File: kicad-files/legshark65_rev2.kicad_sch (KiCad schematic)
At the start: 199 parts, among them J1 ARM JTAG, SW1 K2-1187SQ-A4SW-06, SW2 PCM12SMTR, T2 53261-0471, U1 STM32F411CEU6, U2 MCP1700T-3302E/TT, U3 AT24C256C-SSHL-T, Y1 TAXM8M4RFDCET2T

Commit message: Started connecting more stuff
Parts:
- C1, C10, C11, C12, C13, C14, C15, C17, C2, C6, C7, C9: footprint Capacitor_SMD:C_0603_1608Metric_Pad1.08x0.95mm_HandSolder -> Capacitor_SMD:C_0402_1005Metric_Pad0.74x0.62mm_HandSolder
- C3, C5: footprint Capacitor_SMD:C_0603_1608Metric -> Capacitor_SMD:C_0402_1005Metric_Pad0.74x0.62mm_HandSolder
- R1, R11, R15, R5, R6, R7, R8: footprint Resistor_SMD:R_0603_1608Metric -> Resistor_SMD:R_0402_1005Metric_Pad0.72x0.64mm_HandSolder
- R4, R9: footprint Resistor_SMD:R_0402_1005Metric -> Resistor_SMD:R_0402_1005Metric_Pad0.72x0.64mm_HandSolder
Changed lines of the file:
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@@
       (effects (font (size 1.27 1.27)) (justify left))
     )
-    (property "Footprint" "Capacitor_SMD:C_0603_1608Metric_Pad1.08x0.95mm_HandSolder" (at 116.205 205.4352 0)
+    (property "Footprint" "Capacitor_SMD:C_0402_1005Metric_Pad0.74x0.62mm_HandSolder" (at 116.205 205.4352 0)
       (effects (font (size 1.27 1.27)) hide)
     )
@@
       (effects (font (size 1.27 1.27)) (justify left))
     )
-    (property "Footprint" "Capacitor_SMD:C_0603_1608Metric_Pad1.08x0.95mm_HandSolder" (at 104.14 227.6348 0)
+    (property "Footprint" "Capacitor_SMD:C_0402_1005Metric_Pad0.74x0.62mm_HandSolder" (at 104.14 227.6348 0)
       (effects (font (size 1.27 1.27)) hide)
     )
@@
       (effects (font (size 1.27 1.27)) (justify left))
     )
-    (property "Footprint" "Capacitor_SMD:C_0603_1608Metric_Pad1.08x0.95mm_HandSolder" (at 134.62 188.9252 0)
+    (property "Footprint" "Capacitor_SMD:C_0402_1005Metric_Pad0.74x0.62mm_HandSolder" (at 134.62 188.9252 0)
       (effects (font (size 1.27 1.27)) hide)
     )
@@
       (effects (font (size 1.27 1.27)))
     )
-    (property "Footprint" "Resistor_SMD:R_0603_1608Metric" (at 180.848 289.56 90)
+    (property "Footprint" "Resistor_SMD:R_0402_1005Metric_Pad0.72x0.64mm_HandSolder" (at 180.848 289.56 90)
       (effects (font (size 1.27 1.27)) hide)
     )
@@
       (effects (font (size 1.27 1.27)) (justify left))
     )
-    (property "Footprint" "Capacitor_SMD:C_0603_1608Metric_Pad1.08x0.95mm_HandSolder" (at 204.47 297.4848 0)
+    (property "Footprint" "Capacitor_SMD:C_0402_1005Metric_Pad0.74x0.62mm_HandSolder" (at 204.47 297.4848 0)
       (effects (font (size 1.27 1.27)) hide)
     )
@@
       (effects (font (size 1.27 1.27)))
     )
-    (property "Footprint" "Resistor_SMD:R_0603_1608Metric" (at 99.06 182.118 90)
+    (property "Footprint" "Resistor_SMD:R_0402_1005Metric_Pad0.72x0.64mm_HandSolder" (at 99.06 182.118 90)
       (effects (font (size 1.27 1.27)) hide)
     )
@@
       (effects (font (size 1.27 1.27)))
     )
-    (property "Footprint" "Resistor_SMD:R_0603_1608Metric" (at 232.41 222.758 90)
+    (property "Footprint" "Resistor_SMD:R_0402_1005Metric_Pad0.72x0.64mm_HandSolder" (at 232.41 222.758 90)
       (effects (font (size 1.27 1.27)) hide)
     )
@@
       (effects (font (size 1.27 1.27)) (justify left))
     )
-    (property "Footprint" "Capacitor_SMD:C_0603_1608Metric" (at 50.4952 298.45 0)
+    (property "Footprint" "Capacitor_SMD:C_0402_1005Metric_Pad0.74x0.62mm_HandSolder" (at 50.4952 298.45 0)
       (effects (font (size 1.27 1.27)) hide)
     )
@@
       (effects (font (size 1.27 1.27)))
     )
-    (property "Footprint" "Resistor_SMD:R_0402_1005Metric" (at 57.658 294.64 90)
+    (property "Footprint" "Resistor_SMD:R_0402_1005Metric_Pad0.72x0.64mm_HandSolder" (at 57.658 294.64 90)
       (effects (font (size 1.27 1.27)) hide)
     )
@@
       (effects (font (size 1.27 1.27)))
     )
-    (property "Footprint" "Resistor_SMD:R_0402_1005Metric" (at 94.488 294.64 90)
+    (property "Footprint" "Resistor_SMD:R_0402_1005Metric_Pad0.72x0.64mm_HandSolder" (at 94.488 294.64 90)
       (effects (font (size 1.27 1.27)) hide)
     )
@@
       (effects (font (size 1.27 1.27)) (justify left))
     )
-    (property "Footprint" "Capacitor_SMD:C_0603_1608Metric_Pad1.08x0.95mm_HandSolder" (at 192.7352 293.37 0)
+    (property "Footprint" "Capacitor_SMD:C_0402_1005Metric_Pad0.74x0.62mm_HandSolder" (at 192.7352 293.37 0)
       (effects (font (size 1.27 1.27)) hide)
     )
@@
       (effects (font (size 1.27 1.27)) (justify left))
     )
-    (property "Footprint" "Capacitor_SMD:C_0603_1608Metric_Pad1.08x0.95mm_HandSolder" (at 106.9848 180.34 0)
+    (property "Footprint" "Capacitor_SMD:C_0402_1005Metric_Pad0.74x0.62mm_HandSolder" (at 106.9848 180.34 0)
       (effects (font (size 1.27 1.27)) hide)
     )
@@
       (effects (font (size 1.27 1.27)))
     )
-    (property "Footprint" "Resistor_SMD:R_0603_1608Metric" (at 100.33 156.972 90)
+    (property "Footprint" "Resistor_SMD:R_0402_1005Metric_Pad0.72x0.64mm_HandSolder" (at 100.33 156.972 90)
       (effects (font (size 1.27 1.27)) hide)
     )
@@
       (effects (font (size 1.27 1.27)) (justify left))
     )
-    (property "Footprint" "Capacitor_SMD:C_0603_1608Metric_Pad1.08x0.95mm_HandSolder" (at 96.52 235.2548 0)
+    (property "Footprint" "Capacitor_SMD:C_0402_1005Metric_Pad0.74x0.62mm_HandSolder" (at 96.52 235.2548 0)
       (effects (font (size 1.27 1.27)) hide)
     )
@@
       (effects (font (size 1.27 1.27)) (justify left))
     )
-    (property "Footprint" "Capacitor_SMD:C_0603_1608Metric_Pad1.08x0.95mm_HandSolder" (at 107.6452 256.54 0)
+    (property "Footprint" "Capacitor_SMD:C_0402_1005Metric_Pad0.74x0.62mm_HandSolder" (at 107.6452 256.54 0)
       (effects (font (size 1.27 1.27)) hide)
     )
@@
       (effects (font (size 1.27 1.27)))
     )
-    (property "Footprint" "Resistor_SMD:R_0603_1608Metric" (at 171.958 176.53 90)
+    (property "Footprint" "Resistor_SMD:R_0402_1005Metric_Pad0.72x0.64mm_HandSolder" (at 171.958 176.53 90)
       (effects (font (size 1.27 1.27)) hide)
     )
@@
       (effects (font (size 1.27 1.27)))
     )
-    (property "Footprint" "Resistor_SMD:R_0603_1608Metric" (at 226.06 243.713 90)
+    (property "Footprint" "Resistor_SMD:R_0402_1005Metric_Pad0.72x0.64mm_HandSolder" (at 226.06 243.713 90)
       (effects (font (size 1.27 1.27)) hide)
     )
@@
       (effects (font (size 1.27 1.27)) (justify left))
     )
-    (property "Footprint" "Capacitor_SMD:C_0603_1608Metric_Pad1.08x0.95mm_HandSolder" (at 106.9848 161.29 0)
+    (property "Footprint" "Capacitor_SMD:C_0402_1005Metric_Pad0.74x0.62mm_HandSolder" (at 106.9848 161.29 0)
       (effects (font (size 1.27 1.27)) hide)
     )
@@
       (effects (font (size 1.27 1.27)) (justify left))
     )
-    (property "Footprint" "Capacitor_SMD:C_0603_1608Metric_Pad1.08x0.95mm_HandSolder" (at 120.3452 256.54 0)
+    (property "Footprint" "Capacitor_SMD:C_0402_1005Metric_Pad0.74x0.62mm_HandSolder" (at 120.3452 256.54 0)
       (effects (font (size 1.27 1.27)) hide)
     )
@@
       (effects (font (size 1.27 1.27)))
     )
-    (property "Footprint" "Resistor_SMD:R_0603_1608Metric" (at 178.308 176.53 90)
+    (property "Footprint" "Resistor_SMD:R_0402_1005Metric_Pad0.72x0.64mm_HandSolder" (at 178.308 176.53 90)
       (effects (font (size 1.27 1.27)) hide)
     )
@@
       (effects (font (size 1.27 1.27)) (justify left))
     )
-    (property "Footprint" "Capacitor_SMD:C_0603_1608Metric" (at 103.8352 298.45 0)
+    (property "Footprint" "Capacitor_SMD:C_0402_1005Metric_Pad0.74x0.62mm_HandSolder" (at 103.8352 298.45 0)
       (effects (font (size 1.27 1.27)) hide)
     )
@@
       (effects (font (size 1.27 1.27)) (justify left))
     )
-    (property "Footprint" "Capacitor_SMD:C_0603_1608Metric_Pad1.08x0.95mm_HandSolder" (at 225.0948 205.74 0)
+    (property "Footprint" "Capacitor_SMD:C_0402_1005Metric_Pad0.74x0.62mm_HandSolder" (at 225.0948 205.74 0)
       (effects (font (size 1.27 1.27)) hide)
     )
@@
       (effects (font (size 1.27 1.27)) (justify left))
     )
-    (property "Footprint" "Capacitor_SMD:C_0603_1608Metric_Pad1.08x0.95mm_HandSolder" (at 200.66 171.7548 0)
+    (property "Footprint" "Capacitor_SMD:C_0402_1005Metric_Pad0.74x0.62mm_HandSolder" (at 200.66 171.7548 0)
       (effects (font (size 1.27 1.27)) hide)
     )

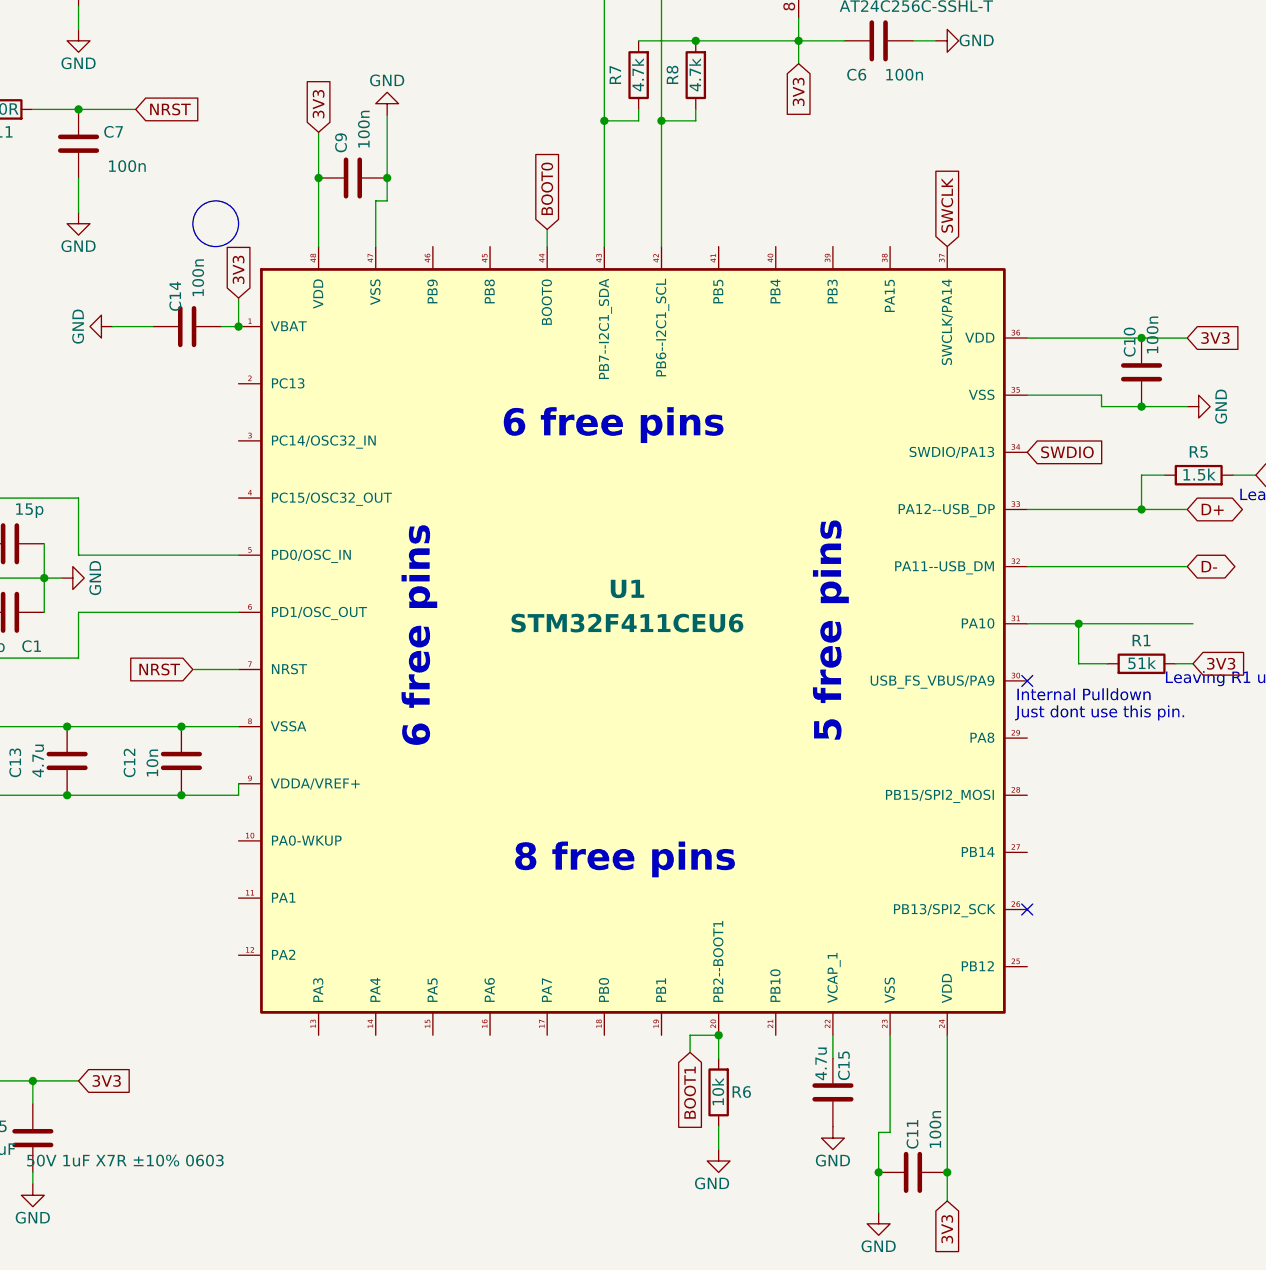
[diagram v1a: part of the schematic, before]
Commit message: Added connections to col and row
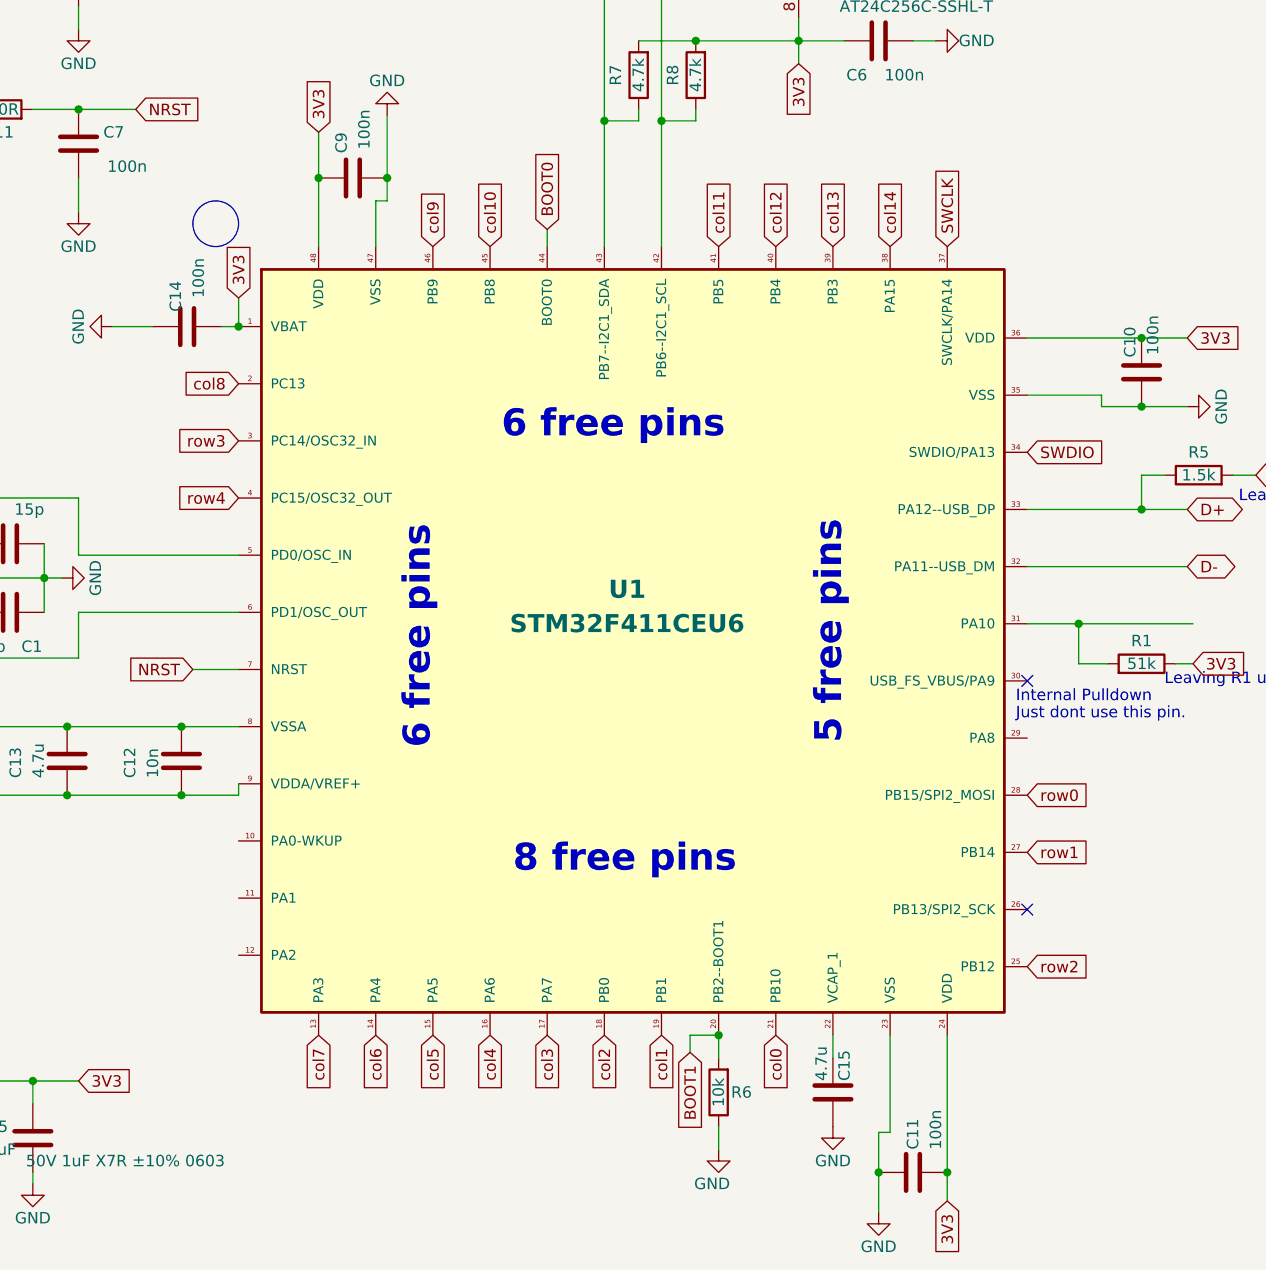
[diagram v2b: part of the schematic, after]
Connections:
- net col0: now also U1.21 (PB10)
- net col1: now also U1.19 (PB1)
- net col10: now also U1.45 (PB8)
- net col11: now also U1.41 (PB5)
- net col12: now also U1.40 (PB4)
- net col13: now also U1.39 (PB3)
- net col14: now also U1.38 (PA15)
- net col2: now also U1.18 (PB0)
- net col3: now also U1.17 (PA7)
- net col4: now also U1.16 (PA6)
- net col5: now also U1.15 (PA5)
- net col6: now also U1.14 (PA4)
- net col7: now also U1.13 (PA3)
- net col8: now also U1.2 (PC13)
- net col9: now also U1.46 (PB9)
- net row0: now also U1.28 (PB15/SPI2_MOSI)
- net row1: now also U1.27 (PB14)
- net row2: now also U1.25 (PB12)
- net row3: now also U1.3 (PC14/OSC32_IN)
- net row4: now also U1.4 (PC15/OSC32_OUT)
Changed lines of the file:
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@@
+    )
+  )
+  (global_label "row4" (shape input) (at 125.73 223.52 180)
+    (effects (font (size 1.27 1.27)) (justify right))
+    (property "Intersheetrefs" "${INTERSHEET_REFS}" (at 125.73 223.52 0)
+      (effects (font (size 1.27 1.27)) hide)
+    )
+  )
+  (global_label "col2" (shape input) (at 166.37 283.21 270)
+    (effects (font (size 1.27 1.27)) (justify right))
+    (property "Intersheetrefs" "${INTERSHEET_REFS}" (at 166.37 283.21 0)
+      (effects (font (size 1.27 1.27)) hide)
+    )
+  )
+  (global_label "col7" (shape input) (at 134.62 283.21 270)
+    (effects (font (size 1.27 1.27)) (justify right))
+    (property "Intersheetrefs" "${INTERSHEET_REFS}" (at 134.62 283.21 0)
+      (effects (font (size 1.27 1.27)) hide)
+    )
+  )
+  (global_label "row0" (shape input) (at 213.36 256.54 0)
+    (effects (font (size 1.27 1.27)) (justify left))
+    (property "Intersheetrefs" "${INTERSHEET_REFS}" (at 213.36 256.54 0)
+      (effects (font (size 1.27 1.27)) hide)
     )
   )
@@
     )
   )
+  (global_label "col3" (shape input) (at 160.02 283.21 270)
+    (effects (font (size 1.27 1.27)) (justify right))
+    (property "Intersheetrefs" "${INTERSHEET_REFS}" (at 160.02 283.21 0)
+      (effects (font (size 1.27 1.27)) hide)
+    )
+  )
   (global_label "3V3" (shape input) (at 52.07 175.895 90) (fields_autoplaced)
     (effects (font (size 1.27 1.27)) (justify left))
@@
     )
   )
+  (global_label "col14" (shape input) (at 198.12 195.58 90)
+    (effects (font (size 1.27 1.27)) (justify left))
+    (property "Intersheetrefs" "${INTERSHEET_REFS}" (at 198.12 195.58 0)
+      (effects (font (size 1.27 1.27)) hide)
+    )
+  )
+  (global_label "col1" (shape input) (at 172.72 283.21 270)
+    (effects (font (size 1.27 1.27)) (justify right))
+    (property "Intersheetrefs" "${INTERSHEET_REFS}" (at 172.72 283.21 0)
+      (effects (font (size 1.27 1.27)) hide)
+    )
+  )
   (global_label "SWCLK" (shape input) (at 204.47 195.58 90) (fields_autoplaced)
     (effects (font (size 1.27 1.27)) (justify left))
@@
     )
   )
+  (global_label "col13" (shape input) (at 191.77 195.58 90)
+    (effects (font (size 1.27 1.27)) (justify left))
+    (property "Intersheetrefs" "${INTERSHEET_REFS}" (at 191.77 195.58 0)
+      (effects (font (size 1.27 1.27)) hide)
+    )
+  )
   (global_label "3V3" (shape input) (at 55.245 215.9 0) (fields_autoplaced)
     (effects (font (size 1.27 1.27)) (justify left))
@@
     )
   )
+  (global_label "col4" (shape input) (at 153.67 283.21 270)
+    (effects (font (size 1.27 1.27)) (justify right))
+    (property "Intersheetrefs" "${INTERSHEET_REFS}" (at 153.67 283.21 0)
+      (effects (font (size 1.27 1.27)) hide)
+    )
+  )
   (global_label "3V3" (shape input) (at 97.79 256.54 180) (fields_autoplaced)
     (effects (font (size 1.27 1.27)) (justify right))
@@
     )
   )
+  (global_label "col8" (shape input) (at 125.73 210.82 180)
+    (effects (font (size 1.27 1.27)) (justify right))
+    (property "Intersheetrefs" "${INTERSHEET_REFS}" (at 125.73 210.82 0)
+      (effects (font (size 1.27 1.27)) hide)
+    )
+  )
   (global_label "col13" (shape input) (at 375.92 16.51 180)
     (effects (font (size 1.27 1.27)) (justify right))
@@
     )
   )
+  (global_label "row1" (shape input) (at 213.36 262.89 0)
+    (effects (font (size 1.27 1.27)) (justify left))
+    (property "Intersheetrefs" "${INTERSHEET_REFS}" (at 213.36 262.89 0)
+      (effects (font (size 1.27 1.27)) hide)
+    )
+  )
   (global_label "SWDIO" (shape input) (at 42.545 208.28 180) (fields_autoplaced)
     (effects (font (size 1.27 1.27)) (justify right))
@@
     )
   )
+  (global_label "row3" (shape input) (at 125.73 217.17 180)
+    (effects (font (size 1.27 1.27)) (justify right))
+    (property "Intersheetrefs" "${INTERSHEET_REFS}" (at 125.73 217.17 0)
+      (effects (font (size 1.27 1.27)) hide)
+    )
+  )
+  (global_label "col6" (shape input) (at 140.97 283.21 270)
+    (effects (font (size 1.27 1.27)) (justify right))
+    (property "Intersheetrefs" "${INTERSHEET_REFS}" (at 140.97 283.21 0)
+      (effects (font (size 1.27 1.27)) hide)
+    )
+  )
   (global_label "3V3" (shape input) (at 187.96 175.26 270) (fields_autoplaced)
     (effects (font (size 1.27 1.27)) (justify right))
@@
     )
   )
+  (global_label "col0" (shape input) (at 185.42 283.21 270)
+    (effects (font (size 1.27 1.27)) (justify right))
+    (property "Intersheetrefs" "${INTERSHEET_REFS}" (at 185.42 283.21 0)
+      (effects (font (size 1.27 1.27)) hide)
+    )
+  )
+  (global_label "col12" (shape input) (at 185.42 195.58 90)
+    (effects (font (size 1.27 1.27)) (justify left))
+    (property "Intersheetrefs" "${INTERSHEET_REFS}" (at 185.42 195.58 0)
+      (effects (font (size 1.27 1.27)) hide)
+    )
+  )
   (global_label "col11" (shape input) (at 325.12 16.51 180)
     (effects (font (size 1.27 1.27)) (justify right))
@@
     )
   )
+  (global_label "col10" (shape input) (at 153.67 195.58 90)
+    (effects (font (size 1.27 1.27)) (justify left))
+    (property "Intersheetrefs" "${INTERSHEET_REFS}" (at 153.67 195.58 0)
+      (effects (font (size 1.27 1.27)) hide)
+    )
+  )
   (global_label "BOOT0" (shape input) (at 160.02 193.675 90) (fields_autoplaced)
     (effects (font (size 1.27 1.27)) (justify left))
@@
     )
   )
+  (global_label "col9" (shape input) (at 147.32 195.58 90)
+    (effects (font (size 1.27 1.27)) (justify left))
+    (property "Intersheetrefs" "${INTERSHEET_REFS}" (at 147.32 195.58 0)
+      (effects (font (size 1.27 1.27)) hide)
+    )
+  )
   (global_label "col14" (shape input) (at 401.32 16.51 180)
     (effects (font (size 1.27 1.27)) (justify right))
@@
     )
   )
+  (global_label "col11" (shape input) (at 179.07 195.58 90)
+    (effects (font (size 1.27 1.27)) (justify left))
+    (property "Intersheetrefs" "${INTERSHEET_REFS}" (at 179.07 195.58 0)
+      (effects (font (size 1.27 1.27)) hide)
+    )
+  )
   (global_label "SWDIO" (shape input) (at 213.36 218.44 0) (fields_autoplaced)
     (effects (font (size 1.27 1.27)) (justify left))
@@
     )
   )
+  (global_label "col5" (shape input) (at 147.32 283.21 270)
+    (effects (font (size 1.27 1.27)) (justify right))
+    (property "Intersheetrefs" "${INTERSHEET_REFS}" (at 147.32 283.21 0)
+      (effects (font (size 1.27 1.27)) hide)
+    )
+  )
   (global_label "col1" (shape input) (at 71.12 16.51 180)
     (effects (font (size 1.27 1.27)) (justify right))
@@
       (effects (font (size 1.27 1.27)) hide)
     )
+  )
+  (global_label "row2" (shape input) (at 213.36 275.59 0)
+    (effects (font (size 1.27 1.27)) (justify left))
+    (property "Intersheetrefs" "${INTERSHEET_REFS}" (at 213.36 275.59 0)
+      (effects (font (size 1.27 1.27)) hide)
+    )
